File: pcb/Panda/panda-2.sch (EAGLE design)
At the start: 139 parts, among them IC1 MCP4261-103E/SL, IC2 4040D, IC3 LMC555_SOIC, IC4 74HC00_SOIC, J1 ST-Link, J11 VIN, J12 ACC, J13 SS-52400-003, J14 Power Select, J2 SWIM, J3 ST_3.3V, J4 ST_5V, J5 USART2, J6 USB_A_SMT_FEMALE, J7 Startup Hacks, J8 Boot, K1 G6K-2P-Y, Q1 220mA/50V/3.5Ω, Q10 200mA/40V, Q11 200mA/40V, Q12 220mA/50V/3.5Ω, Q2 220mA/50V/3.5Ω, Q3 220mA/50V/3.5Ω, Q4 220mA/50V/3.5Ω, Q5 220mA/50V/3.5Ω, Q6 220mA/50V/3.5Ω, Q7 220mA/50V/3.5Ω, Q8 220mA/50V/3.5Ω, Q9 200mA/40V, SW1 Reset, SW2 Boot, U1 RASPBERRYPI4_4GB, U10 ACT1210D, U11 ACT1210D, U12 PESD2CANFD27V-T, U13 PESD2CANFD27V-T, U14 PESD2CANFD27V-T, U15 PESD2CANFD27V-T, U16 STM32H723ZGT, U17 MCP4261-103E/ML, U2 USBLC6-4SC6Y, U3 ST1L05CPU33R, U4 TLE9251VSJXUMA1, U5 TLE9251VSJXUMA1, U6 TLE9251VSJXUMA1, U7 TLE9251VSJXUMA1, U8 ACT1210D, U9 ACT1210D, X1 NX2016SA-32MHZ-EXS00A-CS06654

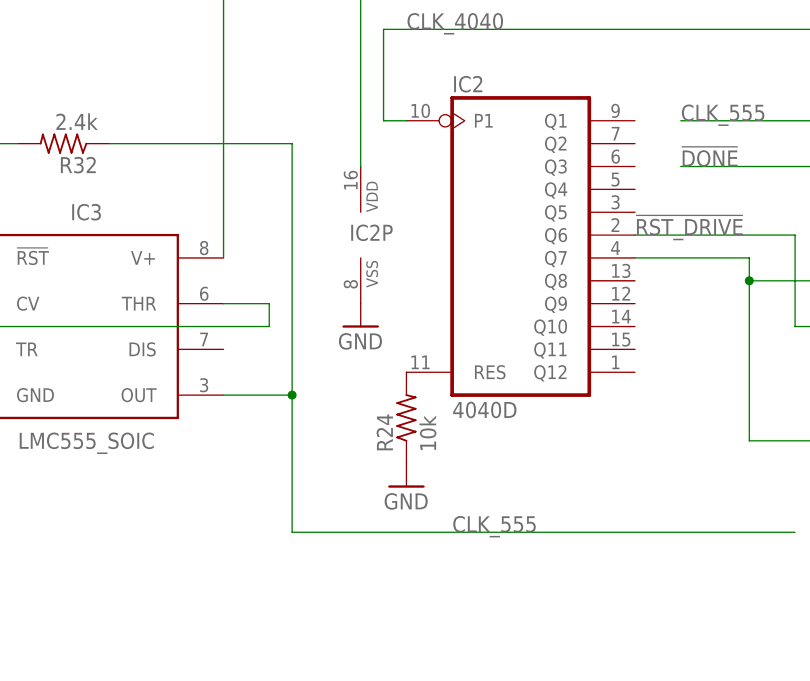
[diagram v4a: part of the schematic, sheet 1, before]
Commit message: Updated PSB design by adding a capacitor to the startup hacks circuit, jsut incase it ever gets built again(it wont)
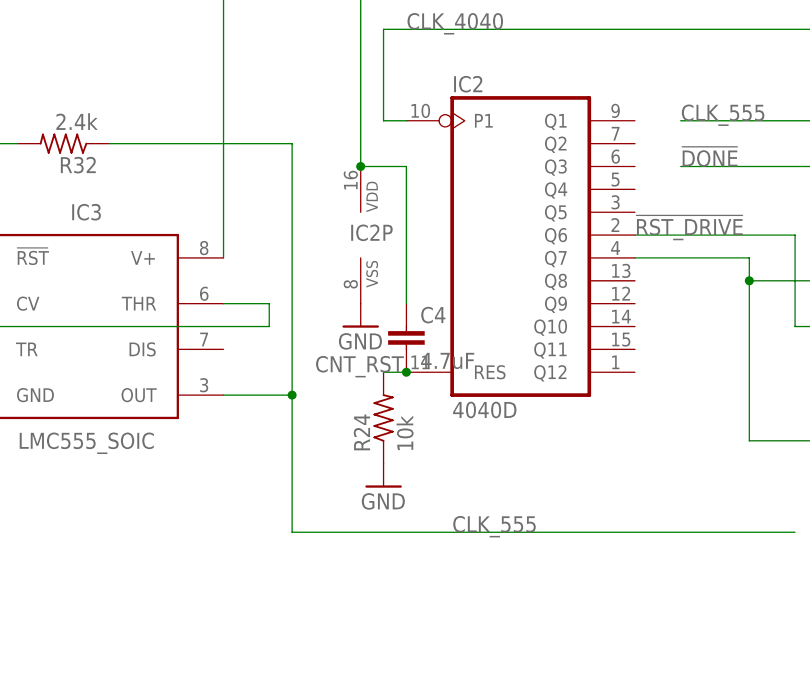
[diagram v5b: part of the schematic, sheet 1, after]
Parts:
- added C4: 4.7uF, rcl:C-EUC0603
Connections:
- removed net N$34: IC2A.RES, R24.2
- new net CNT_RST: C4.2, IC2A.RES, R24.2
- net VHAX: now also C4.1
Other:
- moved on the sheet: R24
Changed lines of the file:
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@@
 <part name="C3" library="rcl" library_urn="urn:adsk.eagle:library:334" deviceset="C-EU" device="C0402" package3d_urn="urn:adsk.eagle:package:23626/2" value="1uF"/>
 <part name="IC3" library="Tinkercad" library_urn="urn:adsk.eagle:library:30890021" deviceset="*555" device="_SOIC" package3d_urn="urn:adsk.eagle:package:18494142/1" technology="LMC"/>
+<part name="C4" library="rcl" library_urn="urn:adsk.eagle:library:334" deviceset="C-EU" device="C0603" package3d_urn="urn:adsk.eagle:package:23616/2" value="4.7uF"/>
 </parts>
 <sheets>
@@
 <attribute name="VALUE" x="137.16" y="185.42" size="1.778" layer="96"/>
 </instance>
-<instance part="R24" gate="G$1" x="132.08" y="185.42" smashed="yes" rot="R90">
-<attribute name="NAME" x="130.5814" y="181.61" size="1.778" layer="95" rot="R90"/>
-<attribute name="VALUE" x="135.382" y="181.61" size="1.778" layer="96" rot="R90"/>
-</instance>
-<instance part="GND66" gate="1" x="132.08" y="177.8" smashed="yes">
-<attribute name="VALUE" x="129.54" y="175.26" size="1.778" layer="96"/>
+<instance part="R24" gate="G$1" x="129.54" y="185.42" smashed="yes" rot="R90">
+<attribute name="NAME" x="128.0414" y="181.61" size="1.778" layer="95" rot="R90"/>
+<attribute name="VALUE" x="132.842" y="181.61" size="1.778" layer="96" rot="R90"/>
+</instance>
+<instance part="GND66" gate="1" x="129.54" y="177.8" smashed="yes">
+<attribute name="VALUE" x="127" y="175.26" size="1.778" layer="96"/>
 </instance>
 <instance part="C1" gate="G$1" x="71.12" y="180.34" smashed="yes">
@@
 <attribute name="NAME" x="96.52" y="208.28" size="1.778" layer="95" align="center"/>
 <attribute name="VALUE" x="96.52" y="182.88" size="1.778" layer="96" align="center"/>
+</instance>
+<instance part="C4" gate="G$1" x="132.08" y="195.58" smashed="yes">
+<attribute name="NAME" x="133.604" y="195.961" size="1.778" layer="95"/>
+<attribute name="VALUE" x="133.604" y="190.881" size="1.778" layer="96"/>
 </instance>
 </instances>
@@
 </segment>
 </net>
-<net name="N$34" class="0">
+<net name="CNT_RST" class="0">
 <segment>
 <pinref part="IC2" gate="A" pin="RES"/>
 <pinref part="R24" gate="G$1" pin="2"/>
+<wire x1="129.54" y1="190.5" x2="132.08" y2="190.5" width="0.1524" layer="91"/>
+<label x="121.92" y="190.5" size="1.778" layer="95"/>
+<pinref part="C4" gate="G$1" pin="2"/>
+<junction x="132.08" y="190.5"/>
 </segment>
 </net>
@@
 <pinref part="IC3" gate="G$1" pin="!RST"/>
 <pinref part="IC3" gate="G$1" pin="V+"/>
-</segment>
-<segment>
+<wire x1="127" y1="213.36" x2="132.08" y2="213.36" width="0.1524" layer="91"/>
+<junction x="127" y="213.36"/>
+<pinref part="C4" gate="G$1" pin="1"/>
+<wire x1="132.08" y1="213.36" x2="132.08" y2="198.12" width="0.1524" layer="91"/>
+</segment>
+<segment>
